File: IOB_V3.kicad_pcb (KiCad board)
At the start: 4 copper layers, 80 x 140 mm, 266 parts, among them J1 Conn_01x02, J10 Conn_01x04, J11 Conn_01x04, J12 Conn_01x04, J13 Conn_01x04, J14 Conn_01x04, J15 Conn_01x08, J16 Conn_02x04_Odd_Even, J17 TFC-103-01-F-D, J18 Conn_01x08, J19 TFC-103-01-F-D, J2 Conn_01x03, J3 Conn_01x04, J4 Conn_01x04, J5 Conn_01x04, J6 Conn_01x04, J7 Conn_01x04, J8 Conn_01x04, J9 Conn_01x04, Q1 BSZ0902NSATMA1, Q10 BSZ0902NSATMA1, Q11 BSZ0902NSATMA1, Q12 BSZ0902NSATMA1, Q13 SI2300, Q2 BSZ0902NSATMA1, Q3 BSZ0902NSATMA1, Q4 BSZ0902NSATMA1, Q5 BSZ0902NSATMA1, Q6 BSZ0902NSATMA1, Q7 BSZ0902NSATMA1, Q8 BSZ0902NSATMA1, Q9 BSZ0902NSATMA1, SW1 SW_Push_Dual, SW2 SW_Push_Dual, SW3 SW_DIP_x08, U1 REF3033, U10 INA180, U11 INA180, U12 INA180, U13 INA180, U14 TS30041, U15 MCP1700-3302E_SOT23, U16 CD74HC4067M, U17 MCP2562FD, U18 W25Q256JV, U19 STM32G474MET3, U2 INA180, U20 CD74HC4067M, U3 INA180, U4 INA180, U5 INA180, U6 INA180, U7 INA180, U8 INA180, U9 INA180, X1 TXC-7C

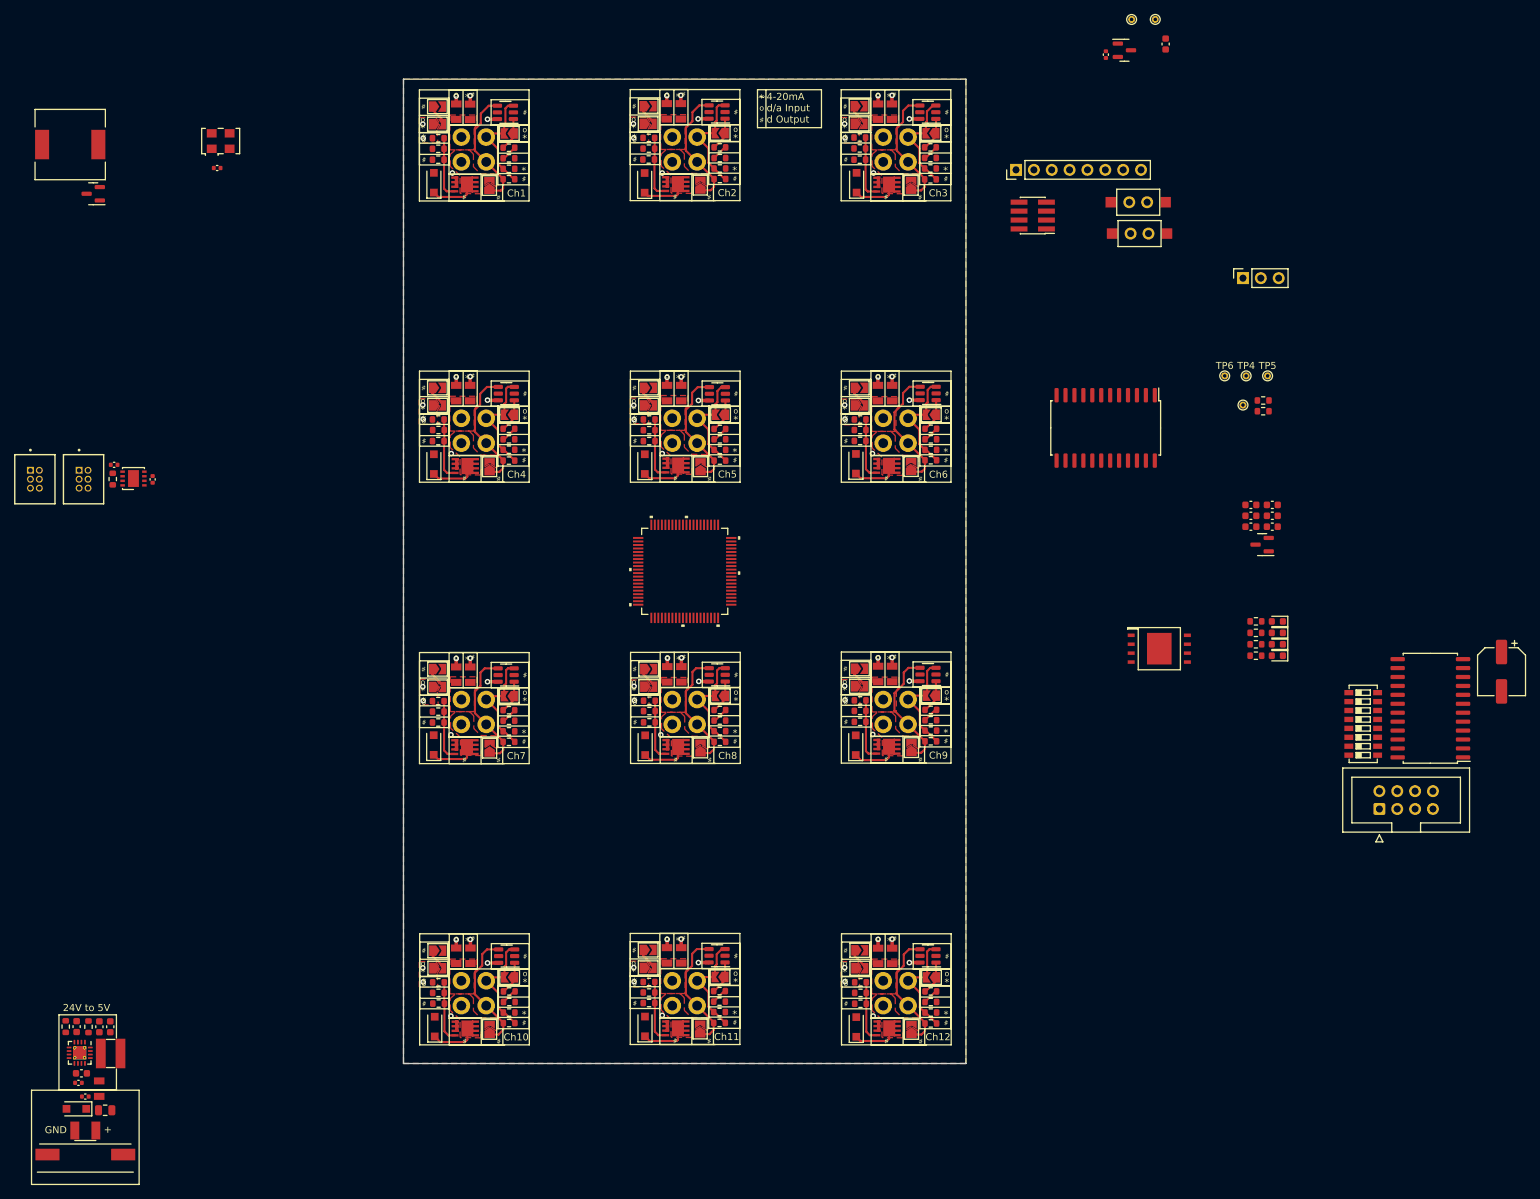
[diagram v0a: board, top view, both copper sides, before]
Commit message: Routing basics done
All layers + the basic layout is already set
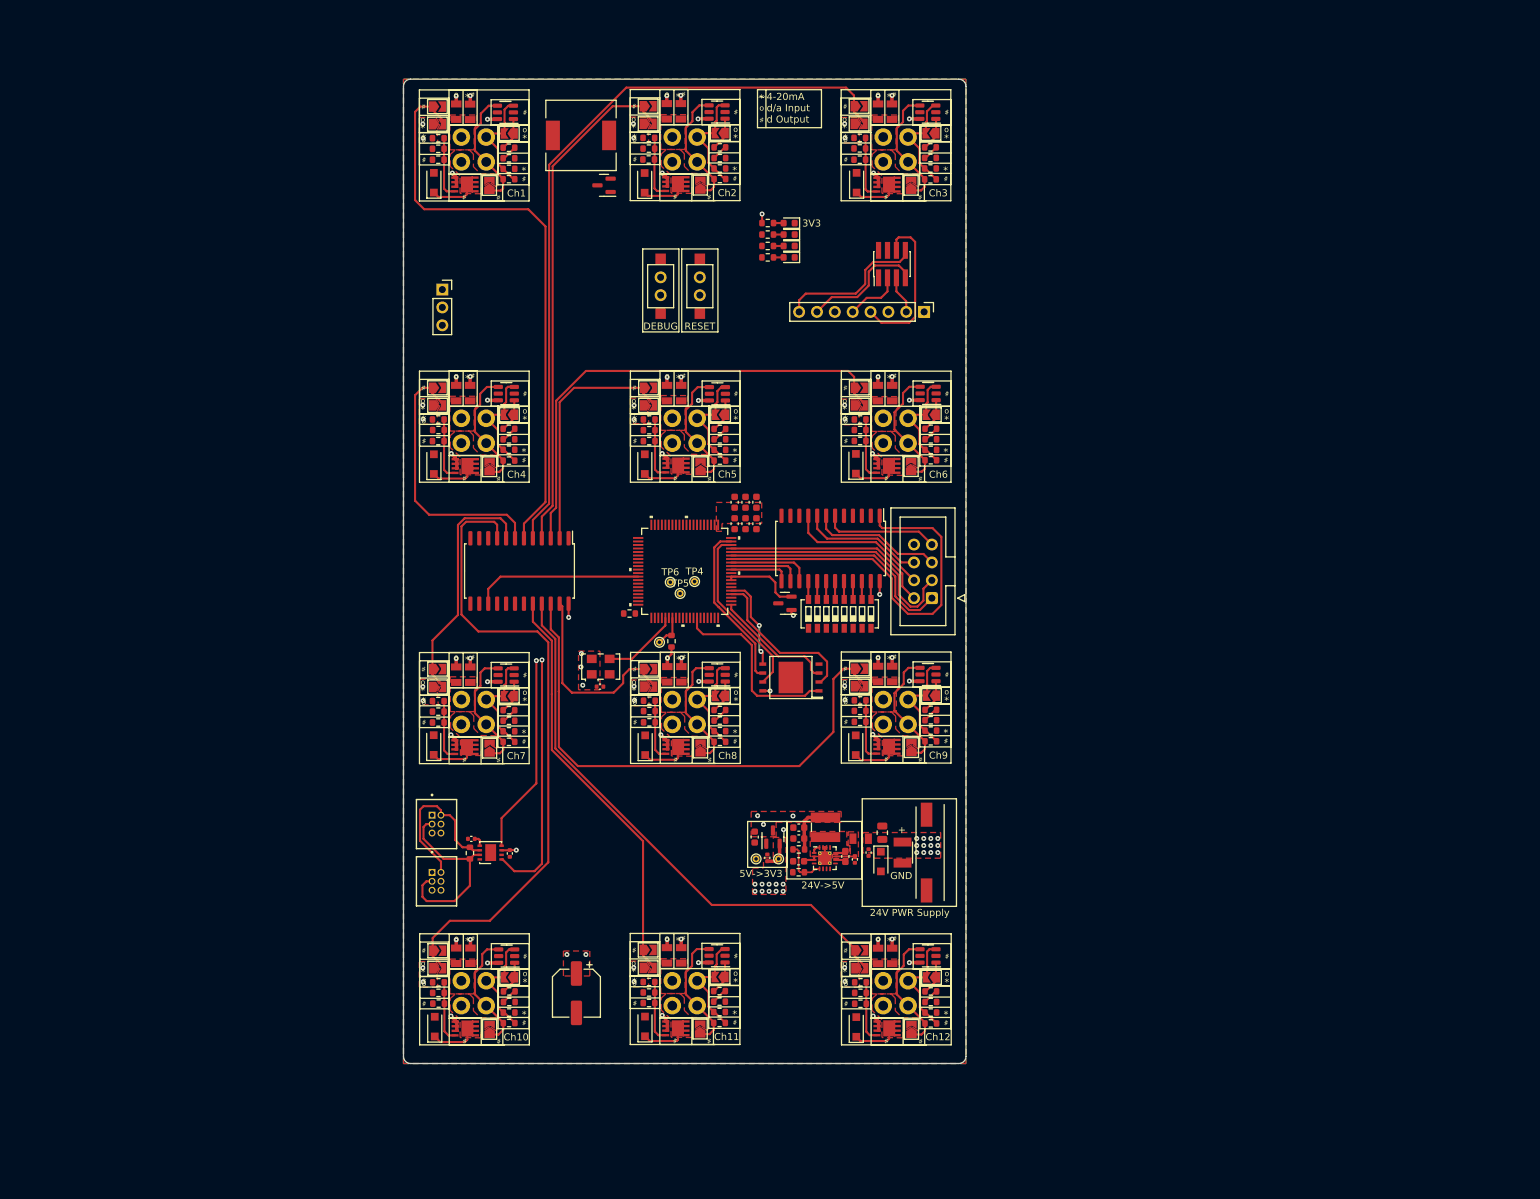
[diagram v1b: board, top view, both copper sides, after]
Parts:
- moved C14 139.3 mm to (94.6, 160.0)
- moved TP3 130.9 mm to (123.3, 140.9), turned to 90 degrees
- moved TP1 130.8 mm to (120.2, 140.9), turned to 90 degrees
- moved J1 127.1 mm to (144.4, 140.0), turned to 90 degrees
- moved C8 127.0 mm to (120.0, 137.8), turned to -90 degrees
- moved C11 124.0 mm to (121.8, 140.8)
- moved U15 122.6 mm to (122.5, 137.8), turned to 90 degrees
- moved D1 119.7 mm to (137.9, 141.3), turned to -90 degrees
- moved C2 117.4 mm to (138.1, 137.2), turned to 90 degrees
- moved C1 116.7 mm to (136.2, 140.0), turned to -90 degrees
- moved C3 114.9 mm to (134.2, 141.0), turned to 90 degrees
- moved F25 114.0 mm to (135.0, 138.0), turned to 0 degrees
- moved J2 113.9 mm to (75.5, 59.9), turned to 0 degrees
- moved C5 112.9 mm to (132.8, 140.6), turned to -90 degrees
- moved U14 109.5 mm to (129.9, 140.8), turned to 0 degrees
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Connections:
- U16 pad 7: /MCU/SPI4_NSS3 -> /MCU/SPI4_NSS2
- U16 pad 8: /MCU/SPI4_NSS2 -> /MCU/SPI4_NSS3
- U19 pad 31: /MCU/MUX1_SEL2 -> /MCU/MUX1_SEL3
- U19 pad 32: /MCU/MUX1_SEL3 -> /MCU/MUX1_SEL2
- U20 pad 2: /Select8 -> /Select5
- U20 pad 20: /Select12 -> /Select11
- U20 pad 21: /Select11 -> /Select12
- U20 pad 22: /Select10 -> /Select9
- U20 pad 23: /Select9 -> /Select8
- U20 pad 3: /Select7 -> /Select6
- U20 pad 4: /Select6 -> /Select2
- U20 pad 5: /Select5 -> /Select3
- U20 pad 6: /Select4 -> /Select1
- U20 pad 7: /Select3 -> /Select4
- U20 pad 8: /Select2 -> /Select7
- U20 pad 9: /Select1 -> /Select10
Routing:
- net +5V: track 0.00 -> 171.2 mm, vias 0 -> 7
- net /Select3: track 3.11 -> 107.1 mm
- net /Select10: track 3.10 -> 91.1 mm
- net /Select1: track 3.10 -> 84.1 mm
- net /Select12: track 3.15 -> 79.1 mm
- net /Select9: track 3.10 -> 77.3 mm
- net /Select2: track 3.10 -> 73.0 mm
- net /Select6: track 3.10 -> 69.0 mm
- net /MCU/SPI4_NSS: track 0.00 -> 55.8 mm
- net /Select11: track 3.15 -> 58.9 mm
- net /MCU/SPI4_MISO: track 0.00 -> 35.9 mm
- net /MCU/CAN1_TX: track 0.00 -> 35.9 mm, vias 0 -> 1
- net /Select4: track 3.11 -> 38.7 mm
- net /MCU/SPI4_SCK: track 0.00 -> 34.1 mm
- net /Select5: track 3.10 -> 35.2 mm
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- added copper zone on F.Cu, net +24V
- added copper zone on F.Cu, net +5V
- added copper zone on F.Cu, net Net-(C3-Pad2)
- added copper zone on F.Cu, net Net-(C5-Pad1)
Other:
- outline, holes or cut-outs redrawn
- board text added: "24V PWR Supply"
- board text added: "24V->5V"
- board text added: "3V3"
- board text added: "5V->3V3"
- board text added: "DEBUG"
- board text added: "RESET"
- board text removed: "24V to 5V"

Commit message: Routing WIP
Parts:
- moved TP4 13.4 mm to (102.5, 91.4)
- moved TP5 13.4 mm to (100.5, 93.1)
- moved TP6 13.4 mm to (99.1, 91.5)
- moved SW2 4.08 mm to (103.7, 62.3), turned to 180 degrees
- moved SW1 3.24 mm to (113.7, 62.3), turned to 0 degrees
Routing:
- net /MCU/NRST: track 12.8 -> 35.3 mm
- net /MCU/CAN1_TX: track 35.9 -> 54.5 mm, vias 1 -> 2
- net /MCU/CAN1_RX: track 28.4 -> 46.5 mm, vias 1 -> 2
- net GND: track 13.6 -> 26.0 mm, vias 13 -> 23
- net Net-(R93-Pad2): track 0.00 -> 7.94 mm
- net Net-(LS1-Pad2): track 0.00 -> 7.79 mm
- net +3V3: track 42.2 -> 47.9 mm, vias 65 -> 71
- net /MCU/BUTTON_1: track 0.00 -> 2.63 mm
- net /MCU/QUADSPI1_BK1_IO3: track 24.9 -> 26.5 mm
- net /MCU/QUADSPI1_CLK: track 23.9 -> 24.5 mm

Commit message: Routing WIP
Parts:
- moved TP6 17.7 mm to (103.2, 108.7)
- moved TP4 13.7 mm to (98.6, 104.5)
- moved TP5 7.26 mm to (100.9, 85.9)
- moved Q13 5.25 mm to (93.3, 45.2), turned to 90 degrees
- moved C12 1.63 mm to (120.3, 93.3)
- moved C16 1.63 mm to (121.8, 93.3)
- moved C17 1.63 mm to (121.8, 90.2)
- moved C18 1.63 mm to (120.3, 90.2)
- moved C19 1.63 mm to (118.7, 90.2)
- moved C9 1.63 mm to (118.7, 93.3)
- moved U1 0.97 mm to (123.3, 104.8)
- moved TP2 0.86 mm to (105.6, 110.4)
- moved R94 0.10 mm to (108.2, 110.0)
- moved F15 0.10 mm to (107.6, 114.7)
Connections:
- R36 pad 2: /MCU/ADC1_IN8 -> /MCU/ADC3_IN4
- R37 pad 1: /MCU/ADC1_IN8 -> /MCU/ADC3_IN4
- R43 pad 2: /MCU/ADC2_IN5 -> /MCU/ADC1_IN14
- R44 pad 1: /MCU/ADC2_IN5 -> /MCU/ADC1_IN14
- R50 pad 2: /MCU/ADC2_IN11 -> /MCU/ADC1_IN8
- R51 pad 1: /MCU/ADC2_IN11 -> /MCU/ADC1_IN8
- R57 pad 2: /MCU/ADC1_IN14 -> /MCU/ADC2_IN5
- R58 pad 1: /MCU/ADC1_IN14 -> /MCU/ADC2_IN5
- R78 pad 2: /MCU/ADC3_IN4 -> /MCU/ADC2_IN11
- R79 pad 1: /MCU/ADC3_IN4 -> /MCU/ADC2_IN11
- TP5 pad 1: Net-(TP5-Pad1) -> Net-(U19-Pad18)
- U19 pad 18: /En8 -> Net-(U19-Pad18)
- U19 pad 43: /MCU/STATUS_LED_1 -> /MCU/MUX1_SEL1
- U19 pad 44: /MCU/STATUS_LED_2 -> /MCU/MUX1_SEL0
- U19 pad 46: /MCU/INPUT_SELECT -> /En3
- U19 pad 47: /MCU/MUX1_SEL0 -> /MCU/STATUS_LED_1
- U19 pad 48: /MCU/MUX1_SEL1 -> /MCU/STATUS_LED_2
- U19 pad 52: /En10 -> /En6
- U19 pad 56: /MCU/MUX2_SEL0 -> /En2
- U19 pad 57: /MCU/MUX2_SEL1 -> /En1
- U19 pad 58: /MCU/MUX2_SEL2 -> /En4
- U19 pad 59: /En3 -> /MCU/INPUT_SELECT
- U19 pad 60: /MCU/MUX2_SEL3 -> /MCU/Speaker_1
- U19 pad 65: /En4 -> /MCU/MUX2_SEL0
- U19 pad 68: /OneWire -> /MCU/MUX2_SEL1
- U19 pad 69: /En6 -> /OneWire
- U19 pad 70: /En1 -> /En10
- U19 pad 71: /En2 -> /En7
- U19 pad 72: /MCU/MUX2_~{EN} -> /MCU/MUX2_SEL3
- U19 pad 73: /En7 -> /MCU/MUX2_SEL2
- U19 pad 74: Net-(TP4-Pad1) -> /MCU/MUX2_~{EN}
- U19 pad 78: /MCU/Speaker_1 -> Net-(TP4-Pad1)
- U19 pad 8: Net-(TP5-Pad1) -> /En8
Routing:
- net /MCU/ADC2_IN12: track 2.27 -> 106.1 mm
- net /En10: track 0.00 -> 93.2 mm
- net /MCU/ADC2_IN11: track 2.27 -> 91.7 mm, vias 0 -> 2
- net /En1: track 0.00 -> 88.4 mm, vias 0 -> 2
- net /OneWire: track 0.00 -> 71.1 mm
- net /MCU/ADC3_IN4: track 2.27 -> 65.9 mm
- net /MCU/Speaker_1: track 0.00 -> 62.1 mm, vias 0 -> 2
- net /En4: track 0.00 -> 52.5 mm, vias 0 -> 2
- net /En7: track 0.00 -> 51.8 mm
- net /MCU/ADC2_IN5: track 2.27 -> 48.3 mm, vias 0 -> 2
- net /En12: track 0.00 -> 29.2 mm
- net /MCU/MUX2_SEL3: track 0.00 -> 26.6 mm
- net /MCU/MUX2_SEL1: track 0.00 -> 25.4 mm
- net /MCU/MUX2_SEL2: track 0.00 -> 25.4 mm
- net /MCU/MUX2_SEL0: track 0.00 -> 23.3 mm
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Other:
- board text removed: "~"
